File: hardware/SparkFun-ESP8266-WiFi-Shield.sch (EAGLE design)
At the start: 60 parts, among them Q1 BSS138, Q2 BSS138, U1 AP2112K-3.3V, U2 ESP8266, U3 AT25SF041-SOIC8, Y1 26MHz

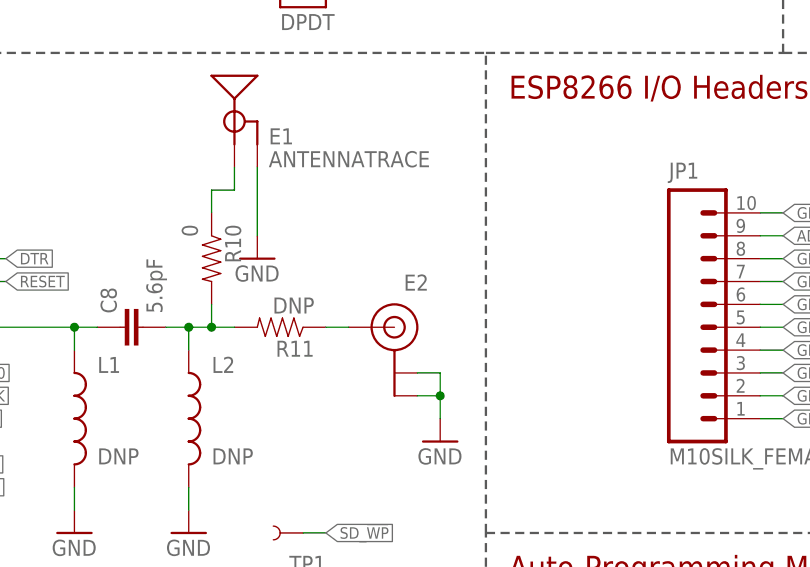
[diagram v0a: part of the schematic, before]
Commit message: Fixing U.FL name and value, minor re-routing.
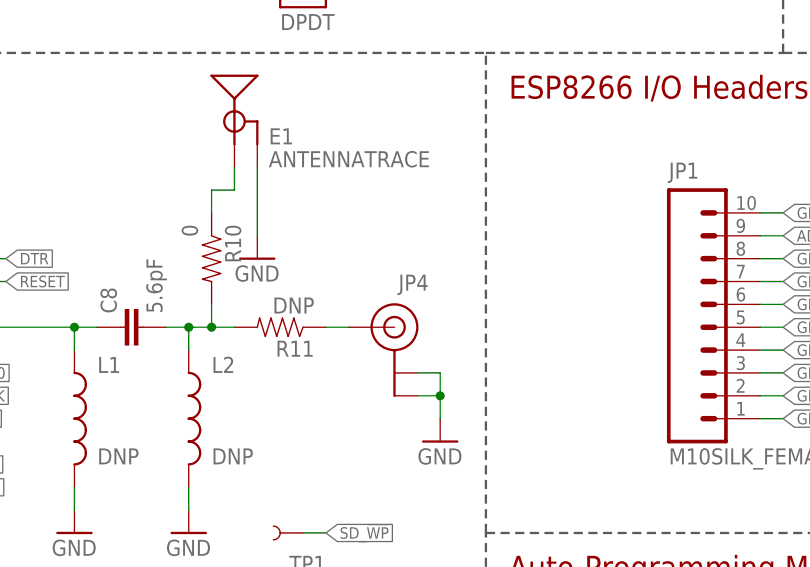
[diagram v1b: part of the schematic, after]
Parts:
- renumbered E2 to JP4
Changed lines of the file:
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@@
 <part name="GND11" library="SparkFun-Aesthetics" deviceset="GND" device=""/>
 <part name="GND13" library="SparkFun-Aesthetics" deviceset="GND" device=""/>
-<part name="E2" library="SparkFun-Connectors" deviceset="U.FL" device="" value="U.FL"/>
 <part name="GND16" library="SparkFun-Aesthetics" deviceset="GND" device=""/>
 <part name="C7" library="SparkFun-Capacitors" deviceset="1.0UF-16V-10%(0603)" device="" value="1.0uF"/>
@@
 <part name="D2" library="SparkFun-LED" deviceset="LED-BLUE" device="0603" value="BLUE"/>
 <part name="SJ3" library="SparkFun-Passives" deviceset="JUMPER-PAD-2-NC_BY_TRACE" device="" value=""/>
+<part name="JP4" library="SparkFun-Connectors" deviceset="U.FL" device="" value="U.FL"/>
 </parts>
 <sheets>
@@
 <instance part="GND11" gate="1" x="101.6" y="68.58"/>
 <instance part="GND13" gate="1" x="114.3" y="68.58"/>
-<instance part="E2" gate="G$1" x="137.16" y="91.44" rot="MR0"/>
 <instance part="GND16" gate="1" x="142.24" y="78.74"/>
 <instance part="C7" gate="G$1" x="88.9" y="99.06" rot="R90"/>
@@
 <instance part="D2" gate="G$1" x="91.44" y="48.26"/>
 <instance part="SJ3" gate="G$1" x="220.98" y="88.9" rot="R180"/>
+<instance part="JP4" gate="G$1" x="137.16" y="91.44" rot="MR0"/>
 </instances>
 <busses>
@@
 <pinref part="GND16" gate="1" pin="GND"/>
 <wire x1="142.24" y1="81.28" x2="142.24" y2="83.82" width="0.1524" layer="91"/>
-<pinref part="E2" gate="G$1" pin="GND@1"/>
 <wire x1="142.24" y1="83.82" x2="139.7" y2="83.82" width="0.1524" layer="91"/>
-<pinref part="E2" gate="G$1" pin="GND@0"/>
 <wire x1="139.7" y1="86.36" x2="142.24" y2="86.36" width="0.1524" layer="91"/>
 <wire x1="142.24" y1="86.36" x2="142.24" y2="83.82" width="0.1524" layer="91"/>
 <junction x="142.24" y="83.82"/>
+<pinref part="JP4" gate="G$1" pin="GND@0"/>
+<pinref part="JP4" gate="G$1" pin="GND@1"/>
 </segment>
 <segment>
@@
 <segment>
 <pinref part="R11" gate="G$1" pin="1"/>
-<pinref part="E2" gate="G$1" pin="SIGNAL"/>
 <wire x1="129.54" y1="91.44" x2="132.08" y2="91.44" width="0.1524" layer="91"/>
-</segment>
-</net>
+<pinref part="JP4" gate="G$1" pin="SIGNAL"/>
+</segment>
+</net>

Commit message: Changing STAT LED to active low.
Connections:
- removed net N$15: D2.C, R6.1
- new net N$9: D2.C, R6.2
- net GND: no longer R6.2
- net GPIO5: now also R6.1; no longer D2.A
- net VCC: now also D2.A
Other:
- note added: "- ESP8266 Booting into Bootloader Mode - Set SJ1 to NO"
- moved on the sheet: D2, R6, R8, TP1, TP2, TP3, TP4, TP5, TP6, TP7
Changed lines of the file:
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@@
 <layer number="255" name="routoute" color="7" fill="1" visible="yes" active="yes"/>
 </layers>
-<schematic xreflabel="%F%N/%S.%C%R" xrefpart="/%S.%C%R">
+<schematic xreflabel="%F%N/%S" xrefpart="/%S.%C%R">
 <attributes>
 </attributes>
@@
 <part name="FID2" library="SparkFun-Aesthetics" deviceset="FIDUCIAL" device="1X2"/>
 <part name="FID1" library="SparkFun-Aesthetics" deviceset="FIDUCIAL" device="1X2"/>
-<part name="GND9" library="SparkFun-Aesthetics" deviceset="GND" device=""/>
 <part name="TP7" library="SparkFun-Passives" deviceset="TEST-POINT" device="3X5" value=""/>
 <part name="LOGO2" library="SparkFun-Aesthetics" deviceset="OSHW-LOGO" device="M" value="OSHW-LOGOM"/>
@@
 <part name="SJ3" library="SparkFun-Passives" deviceset="JUMPER-PAD-2-NC_BY_TRACE" device="" value=""/>
 <part name="JP4" library="SparkFun-Connectors" deviceset="U.FL" device="" value="U.FL"/>
+<part name="SUPPLY15" library="SparkFun-Aesthetics" deviceset="VCC" device=""/>
 </parts>
 <sheets>
@@
 <text x="2.54" y="114.3" size="2.54" layer="94">ESP8266 &amp;
 4 Mbit Flash</text>
+<text x="251.46" y="58.42" size="1.778" layer="97">- ESP8266 Booting into Bootloader Mode
+  - Set SJ1 to NO</text>
 </plain>
 <instances>
@@
 <instance part="FID2" gate="G$1" x="238.76" y="27.94"/>
 <instance part="FID1" gate="G$1" x="236.22" y="25.4"/>
-<instance part="GND9" gate="1" x="91.44" y="25.4"/>
-<instance part="TP7" gate="G$1" x="127" y="38.1" rot="R180"/>
+<instance part="TP7" gate="G$1" x="134.62" y="38.1" rot="R180"/>
 <instance part="LOGO2" gate="G$1" x="71.12" y="12.7"/>
 <instance part="E1" gate="G$1" x="119.38" y="119.38"/>
@@
 <instance part="C5" gate="G$1" x="17.78" y="58.42" rot="MR270"/>
 <instance part="R1" gate="G$1" x="25.4" y="40.64" rot="R90"/>
-<instance part="R6" gate="G$1" x="91.44" y="35.56" rot="R270"/>
+<instance part="R6" gate="G$1" x="86.36" y="53.34"/>
 <instance part="R4" gate="G$1" x="78.74" y="83.82" smashed="yes" rot="R180">
 <attribute name="NAME" x="72.898" y="84.0486" size="1.778" layer="95"/>
 <attribute name="VALUE" x="81.026" y="84.074" size="1.778" layer="96"/>
 </instance>
-<instance part="TP6" gate="G$1" x="127" y="43.18" rot="R180"/>
-<instance part="TP5" gate="G$1" x="127" y="48.26" rot="R180"/>
-<instance part="TP1" gate="G$1" x="127" y="68.58" rot="R180"/>
-<instance part="TP2" gate="G$1" x="127" y="63.5" rot="R180"/>
-<instance part="TP3" gate="G$1" x="127" y="58.42" rot="R180"/>
-<instance part="TP4" gate="G$1" x="127" y="53.34" rot="R180"/>
+<instance part="TP6" gate="G$1" x="134.62" y="43.18" rot="R180"/>
+<instance part="TP5" gate="G$1" x="134.62" y="48.26" rot="R180"/>
+<instance part="TP1" gate="G$1" x="134.62" y="68.58" rot="R180"/>
+<instance part="TP2" gate="G$1" x="134.62" y="63.5" rot="R180"/>
+<instance part="TP3" gate="G$1" x="134.62" y="58.42" rot="R180"/>
+<instance part="TP4" gate="G$1" x="134.62" y="53.34" rot="R180"/>
 <instance part="U1" gate="G$1" x="35.56" y="157.48">
 <attribute name="PROD_ID" x="35.56" y="157.48" size="2.54" layer="96" display="off"/>
@@
 <instance part="R2" gate="G$1" x="63.5" y="144.78" rot="R270"/>
 <instance part="GND8" gate="1" x="63.5" y="134.62"/>
-<instance part="R8" gate="G$1" x="111.76" y="40.64" rot="R90"/>
-<instance part="GND12" gate="1" x="111.76" y="30.48"/>
+<instance part="R8" gate="G$1" x="124.46" y="45.72" rot="R90"/>
+<instance part="GND12" gate="1" x="124.46" y="35.56"/>
 <instance part="SUPPLY13" gate="G$1" x="226.06" y="58.42"/>
 <instance part="D3" gate="G$1" x="220.98" y="43.18" rot="MR0"/>
@@
 <instance part="GND19" gate="1" x="241.3" y="127" rot="MR0"/>
 <instance part="S1" gate="G$1" x="127" y="137.16"/>
-<instance part="D2" gate="G$1" x="91.44" y="48.26"/>
+<instance part="D2" gate="G$1" x="99.06" y="53.34" rot="R270"/>
 <instance part="SJ3" gate="G$1" x="220.98" y="88.9" rot="R180"/>
 <instance part="JP4" gate="G$1" x="137.16" y="91.44" rot="MR0"/>
+<instance part="SUPPLY15" gate="G$1" x="104.14" y="55.88"/>
 </instances>
 <busses>
@@
 <junction x="142.24" y="172.72"/>
 </segment>
+<segment>
+<pinref part="D2" gate="G$1" pin="A"/>
+<pinref part="SUPPLY15" gate="G$1" pin="VCC"/>
+<wire x1="101.6" y1="53.34" x2="104.14" y2="53.34" width="0.1524" layer="91"/>
+<wire x1="104.14" y1="53.34" x2="104.14" y2="55.88" width="0.1524" layer="91"/>
+</segment>
 </net>
 <net name="GND" class="0">
@@
 </segment>
 <segment>
-<pinref part="GND9" gate="1" pin="GND"/>
-<wire x1="91.44" y1="27.94" x2="91.44" y2="30.48" width="0.1524" layer="91"/>
-<pinref part="R6" gate="G$1" pin="2"/>
-</segment>
-<segment>
 <pinref part="E1" gate="G$1" pin="GND"/>
 <pinref part="GND14" gate="1" pin="GND"/>
@@
 <pinref part="R8" gate="G$1" pin="1"/>
 <pinref part="GND12" gate="1" pin="GND"/>
-<wire x1="111.76" y1="33.02" x2="111.76" y2="35.56" width="0.1524" layer="91"/>
+<wire x1="124.46" y1="38.1" x2="124.46" y2="40.64" width="0.1524" layer="91"/>
 </segment>
 <segment>
@@
 <segment>
 <pinref part="TP7" gate="G$1" pin="1"/>
-<wire x1="127" y1="38.1" x2="129.54" y2="38.1" width="0.1524" layer="91"/>
-<label x="129.54" y="38.1" size="1.27" layer="95" xref="yes"/>
+<wire x1="134.62" y1="38.1" x2="137.16" y2="38.1" width="0.1524" layer="91"/>
+<label x="137.16" y="38.1" size="1.27" layer="95" xref="yes"/>
 </segment>
 </net>
@@
 <segment>
 <pinref part="U2" gate="G$1" pin="GPIO5"/>
-<wire x1="71.12" y1="53.34" x2="91.44" y2="53.34" width="0.1524" layer="91"/>
-<wire x1="91.44" y1="53.34" x2="91.44" y2="50.8" width="0.1524" layer="91"/>
-<wire x1="91.44" y1="53.34" x2="93.98" y2="53.34" width="0.1524" layer="91"/>
-<junction x="91.44" y="53.34"/>
-<label x="93.98" y="53.34" size="1.27" layer="95" xref="yes"/>
-<pinref part="D2" gate="G$1" pin="A"/>
+<wire x1="71.12" y1="53.34" x2="81.28" y2="53.34" width="0.1524" layer="91"/>
+<pinref part="R6" gate="G$1" pin="1"/>
 </segment>
 <segment>
@@
 </segment>
 <segment>
-<wire x1="127" y1="68.58" x2="129.54" y2="68.58" width="0.1524" layer="91"/>
-<label x="129.54" y="68.58" size="1.27" layer="95" rot="MR180" xref="yes"/>
+<wire x1="134.62" y1="68.58" x2="137.16" y2="68.58" width="0.1524" layer="91"/>
+<label x="137.16" y="68.58" size="1.27" layer="95" rot="MR180" xref="yes"/>
 <pinref part="TP1" gate="G$1" pin="1"/>
 </segment>
@@
 </segment>
 <segment>
-<wire x1="127" y1="53.34" x2="129.54" y2="53.34" width="0.1524" layer="91"/>
-<label x="129.54" y="53.34" size="1.27" layer="95" rot="MR180" xref="yes"/>
+<wire x1="134.62" y1="53.34" x2="137.16" y2="53.34" width="0.1524" layer="91"/>
+<label x="137.16" y="53.34" size="1.27" layer="95" rot="MR180" xref="yes"/>
 <pinref part="TP4" gate="G$1" pin="1"/>
 </segment>
@@
 </segment>
 <segment>
-<wire x1="127" y1="63.5" x2="129.54" y2="63.5" width="0.1524" layer="91"/>
-<label x="129.54" y="63.5" size="1.27" layer="95" rot="MR180" xref="yes"/>
+<wire x1="134.62" y1="63.5" x2="137.16" y2="63.5" width="0.1524" layer="91"/>
+<label x="137.16" y="63.5" size="1.27" layer="95" rot="MR180" xref="yes"/>
 <pinref part="TP2" gate="G$1" pin="1"/>
 </segment>
@@
 </segment>
 <segment>
-<wire x1="127" y1="48.26" x2="129.54" y2="48.26" width="0.1524" layer="91"/>
-<label x="129.54" y="48.26" size="1.27" layer="95" rot="MR180" xref="yes"/>
+<wire x1="134.62" y1="48.26" x2="137.16" y2="48.26" width="0.1524" layer="91"/>
+<label x="137.16" y="48.26" size="1.27" layer="95" rot="MR180" xref="yes"/>
 <pinref part="TP5" gate="G$1" pin="1"/>
 </segment>
@@
 </segment>
 <segment>
-<wire x1="127" y1="58.42" x2="129.54" y2="58.42" width="0.1524" layer="91"/>
-<label x="129.54" y="58.42" size="1.27" layer="95" rot="MR180" xref="yes"/>
+<wire x1="134.62" y1="58.42" x2="137.16" y2="58.42" width="0.1524" layer="91"/>
+<label x="137.16" y="58.42" size="1.27" layer="95" rot="MR180" xref="yes"/>
 <pinref part="TP3" gate="G$1" pin="1"/>
 </segment>
@@
 </segment>
 <segment>
-<wire x1="127" y1="43.18" x2="129.54" y2="43.18" width="0.1524" layer="91"/>
-<label x="129.54" y="43.18" size="1.27" layer="95" rot="MR180" xref="yes"/>
+<wire x1="134.62" y1="43.18" x2="137.16" y2="43.18" width="0.1524" layer="91"/>
+<label x="137.16" y="43.18" size="1.27" layer="95" rot="MR180" xref="yes"/>
 <pinref part="TP6" gate="G$1" pin="1"/>
 </segment>
@@
 <segment>
 <pinref part="R8" gate="G$1" pin="2"/>
-<wire x1="111.76" y1="45.72" x2="111.76" y2="48.26" width="0.1524" layer="91"/>
-<wire x1="111.76" y1="48.26" x2="109.22" y2="48.26" width="0.1524" layer="91"/>
-<label x="109.22" y="48.26" size="1.27" layer="95" rot="R180" xref="yes"/>
+<wire x1="124.46" y1="50.8" x2="124.46" y2="53.34" width="0.1524" layer="91"/>
+<wire x1="124.46" y1="53.34" x2="121.92" y2="53.34" width="0.1524" layer="91"/>
+<label x="121.92" y="53.34" size="1.27" layer="95" rot="R180" xref="yes"/>
 </segment>
 <segment>
@@
 <wire x1="71.12" y1="83.82" x2="73.66" y2="83.82" width="0.1524" layer="91"/>
 <pinref part="R4" gate="G$1" pin="2"/>
-</segment>
-</net>
-<net name="N$15" class="0">
-<segment>
-<wire x1="91.44" y1="40.64" x2="91.44" y2="43.18" width="0.1524" layer="91"/>
-<pinref part="R6" gate="G$1" pin="1"/>
-<pinref part="D2" gate="G$1" pin="C"/>
 </segment>
 </net>
@@
 </segment>
 </net>
+<net name="N$9" class="0">
+<segment>
+<pinref part="R6" gate="G$1" pin="2"/>
+<pinref part="D2" gate="G$1" pin="C"/>
+<wire x1="93.98" y1="53.34" x2="91.44" y2="53.34" width="0.1524" layer="91"/>
+</segment>
+</net>

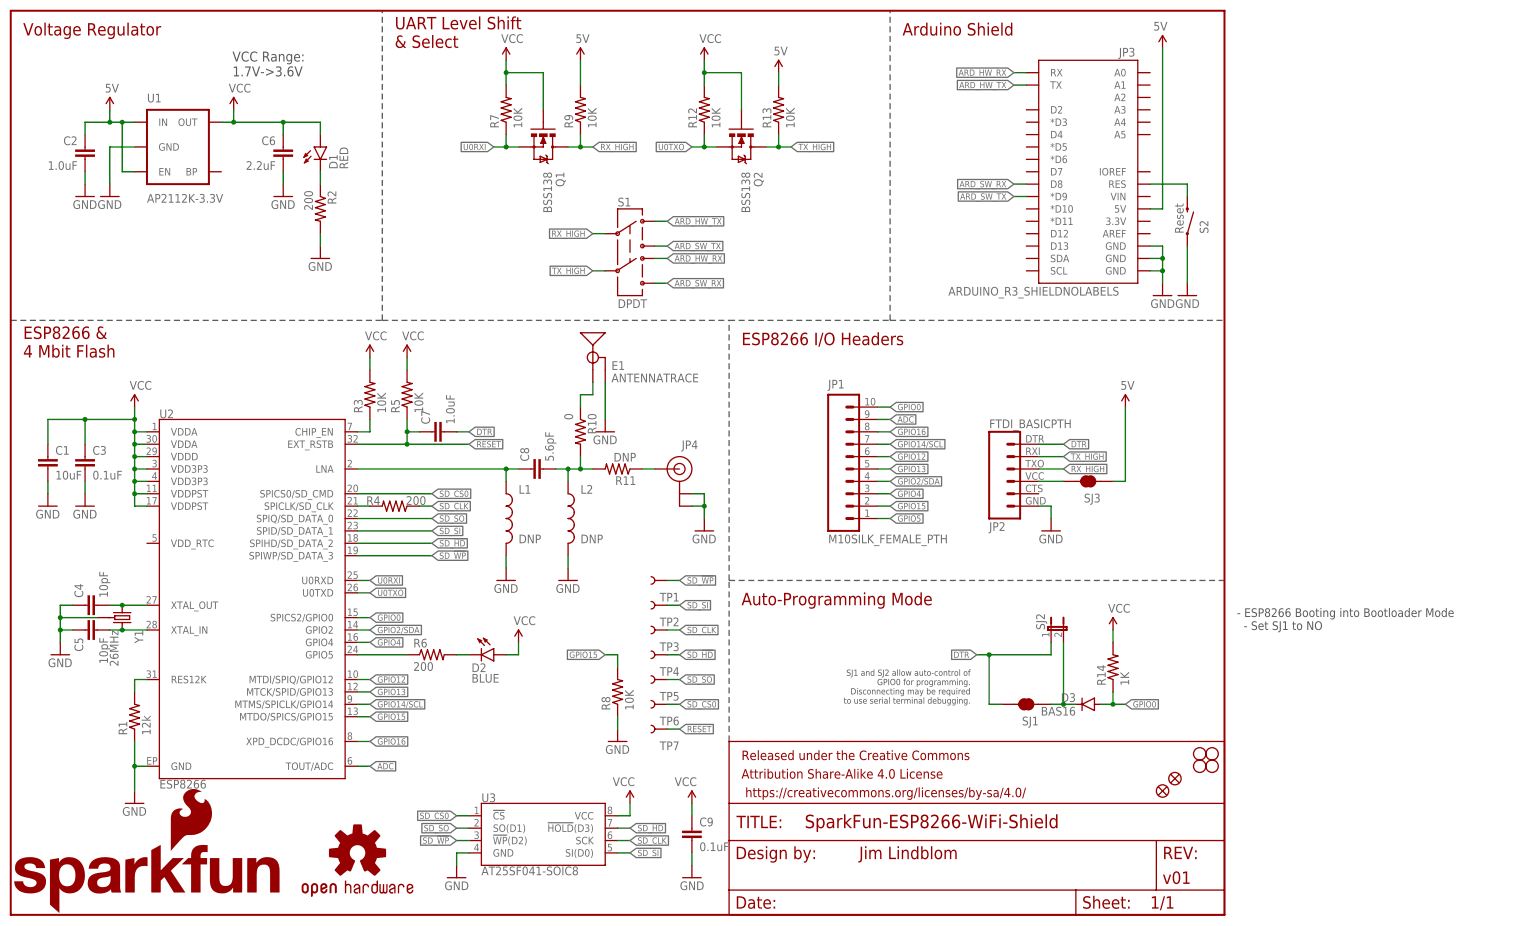
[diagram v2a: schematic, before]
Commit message: Connecting GPIO4 to Arduino RST.
Upping version to v10.
Should allow for remote bootloading.
Jumper in-line to disconnect if necessary.
Defaulting DTR jumpers to open.
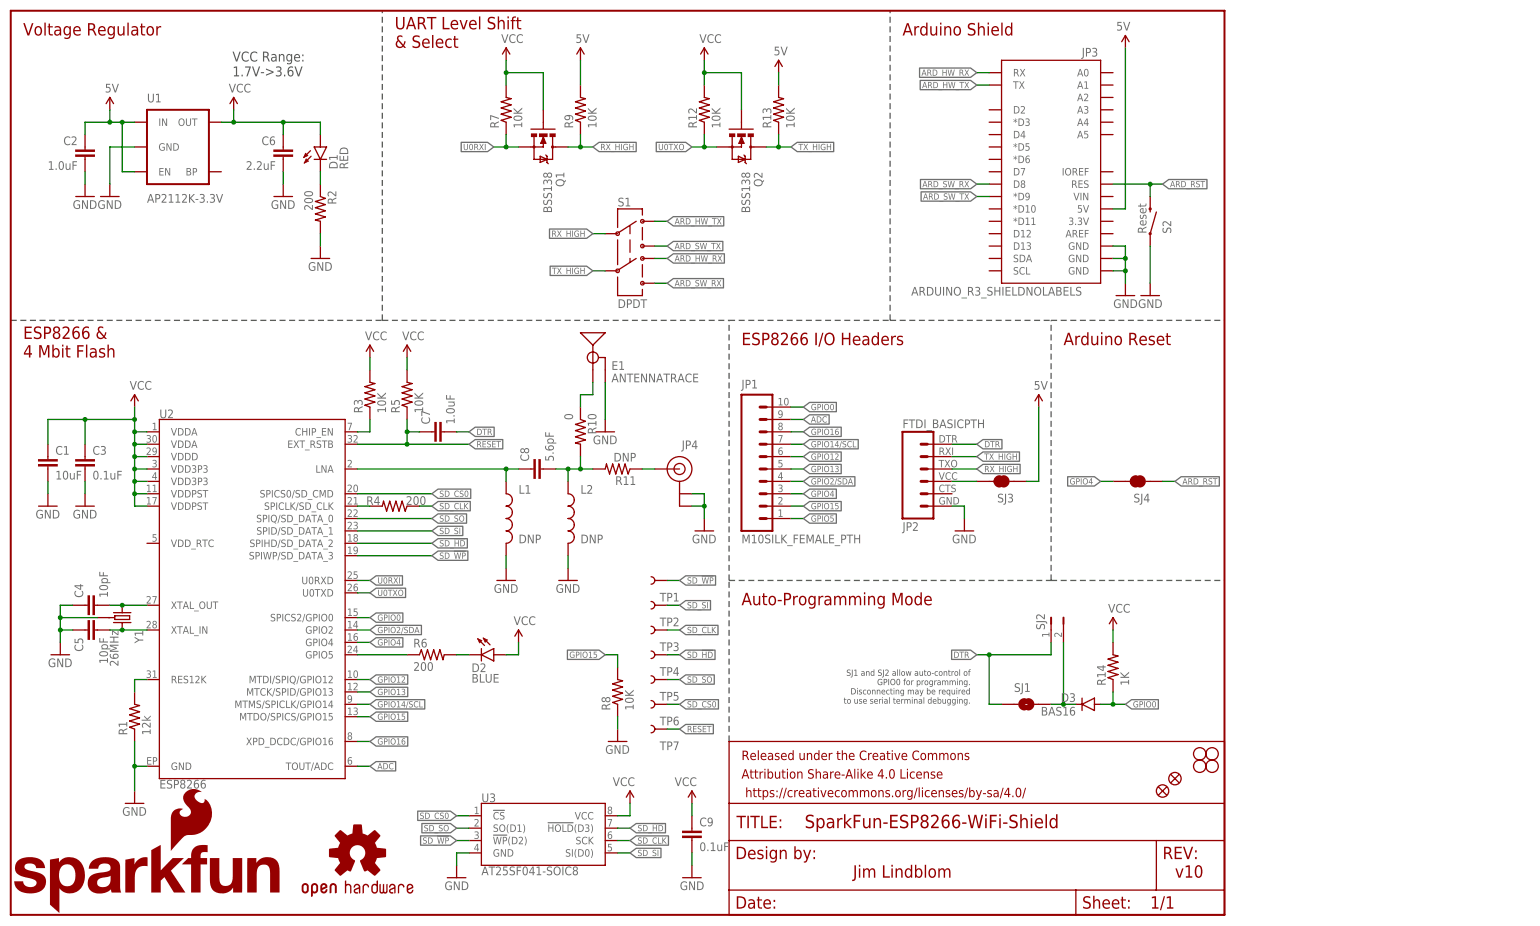
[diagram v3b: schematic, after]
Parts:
- added SJ4: JUMPER-PAD-2-NC_BY_TRACE, SparkFun-Passives:JUMPER-PAD-2-NC_BY_TRACE
- SJ1: value JUMPER-PAD-2-NC_BY_TRACE -> JUMPER-PAD-2-NO; device SparkFun-Passives:JUMPER-PAD-2-NC_BY_TRACE -> SparkFun-Passives:JUMPER-PAD-2-NO
- SJ2: value JUMPER-PTH-2-NC -> JUMPER-PTH-2-NO; device SparkFun-Passives:JUMPER-PTH-2-NC -> SparkFun-Passives:JUMPER-PTH-2-NO
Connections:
- removed net N$8: JP3.RES, S2.2
- new net ARD_RST: JP3.RES, S2.2, SJ4.1
- net DTR: now also SJ1.1; no longer SJ1.2
- net GPIO4: now also SJ4.2
- net SJ2: now also SJ1.2; no longer SJ1.1
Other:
- note added: "Arduino Reset"
- note added: "Jim Lindblom"
- note added: "v10"
- note removed: "- ESP8266 Booting into Bootloader Mode - Set SJ1 to NO"
- moved on the sheet: JP1, JP2, JP3, S2, SJ3

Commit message: Breaking out ESP8266 reset pin.
Moved the FTDI header to avoid interfering with screw head.
Moved position of GPIO5 break out.
Renamed GPIO16 to XPD.
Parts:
- removed JP1: M10SILK_FEMALE_PTH, SparkFun-Connectors:M10SILK_FEMALE_PTH
- added JP6: (no value), SparkFun-Connectors:M11PTH
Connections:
- removed net GPIO14/SCL: JP1.7, U2.MTMS/SPICLK/GPIO14
- removed net GPIO16: JP1.8, U2.XPD_DCDC/GPIO16
- removed net GPIO2/SDA: JP1.4, U2.GPIO2
- new net GPIO14: JP6.8, U2.MTMS/SPICLK/GPIO14
- new net GPIO2: JP6.5, U2.GPIO2
- new net XPD: JP6.9, U2.XPD_DCDC/GPIO16
- net ADC: now also JP6.10; no longer JP1.9
- net GPIO0: now also JP6.11; no longer JP1.10
- net GPIO12: now also JP6.7; no longer JP1.6
- net GPIO13: now also JP6.6; no longer JP1.5
- net GPIO15: now also JP6.3; no longer JP1.2
- net GPIO4: now also JP6.4; no longer JP1.3
- net GPIO5: now also JP6.1; no longer JP1.1
- net RESET: now also JP6.2
